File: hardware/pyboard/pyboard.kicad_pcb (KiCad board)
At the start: 2 copper layers, 65 parts, among them J1 Battery, J2 Arduino_Mega2560_Shield, J6 USB_B_Micro, J9 Micro_SD_SCHA5B0200, Q1 IRLML6402, Q2 IRLML6402, SW1 RST, SW2 USR, U1 STM32F405RGT6, U2 MCP1703A-3302_SOT89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

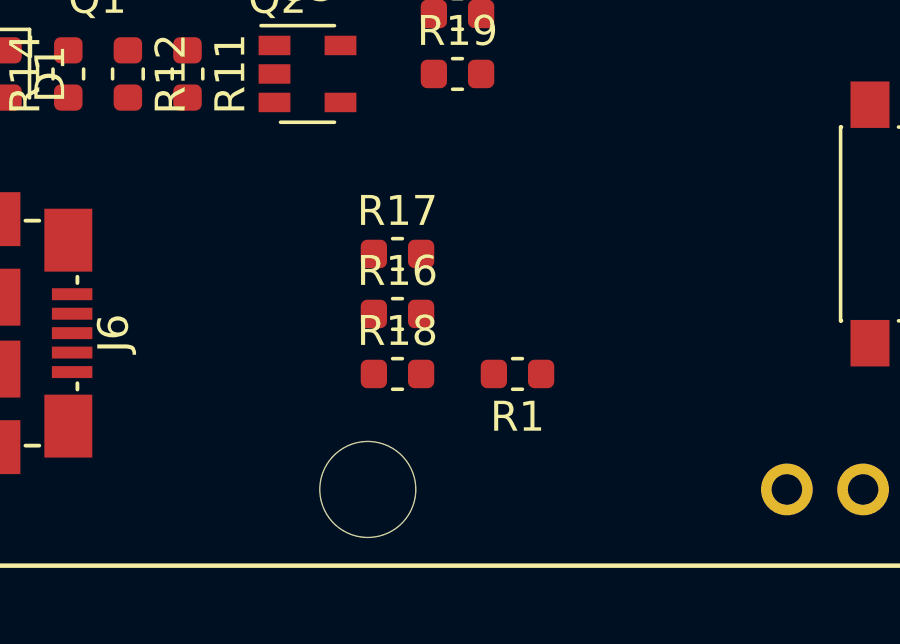
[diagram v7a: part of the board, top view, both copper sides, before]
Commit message: Configure track width
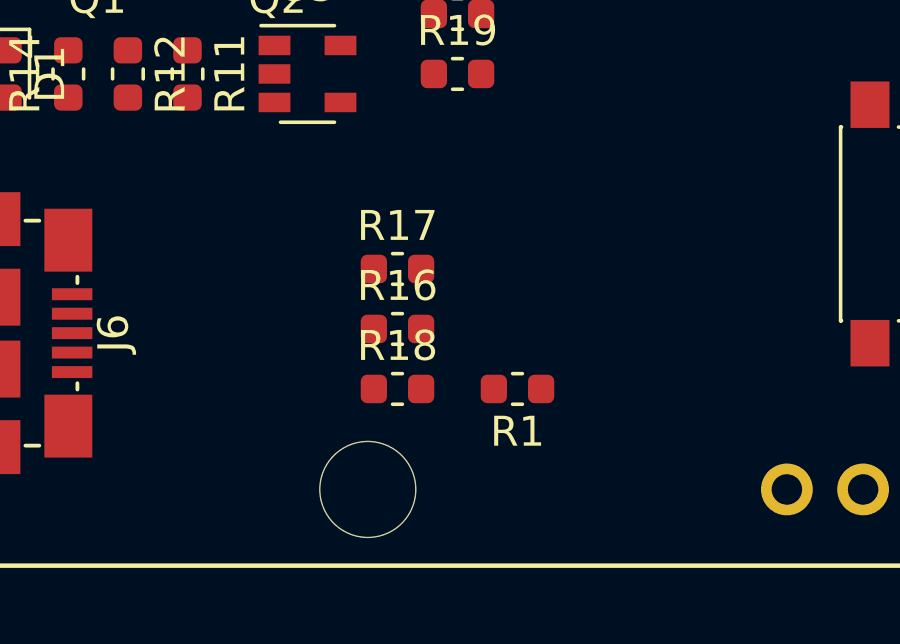
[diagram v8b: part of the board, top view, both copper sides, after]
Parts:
- moved R1 0.50 mm to (119.0, 114.1)
- moved R16 0.50 mm to (115.0, 112.1)
- moved R17 0.50 mm to (115.0, 110.1)
- moved R18 0.50 mm to (115.0, 114.1)
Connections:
- J6 pad D+: (no net) -> /DP_USB
- J6 pad D-: (no net) -> /DM_USB
- J6 pad GND: (no net) -> GND
- J6 pad ID: (no net) -> /ID_USB
- J6 pad VBUS: (no net) -> /VBUS_USB
- R16 pad 1: (no net) -> /DP_USB
- R17 pad 1: (no net) -> /DM_USB
- R18 pad 1: (no net) -> /ID_USB
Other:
- net class Default: trace_width 0.25 -> 0.3
- net class Power added: clearance 0.2, trace_width 0.8, via_dia 0.8, via_drill 0.4
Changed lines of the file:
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@@
     (zones 0)
     (modules 65)
-    (nets 73)
+    (nets 76)
   )
   (page A4)
@@
     (0 F.Cu signal)
     (31 B.Cu signal)
-    (32 B.Adhes user)
     (33 F.Adhes user)
-    (34 B.Paste user)
     (35 F.Paste user)
-    (36 B.SilkS user)
     (37 F.SilkS user)
-    (38 B.Mask user)
     (39 F.Mask user)
     (40 Dwgs.User user)
@@
     (46 B.CrtYd user)
     (47 F.CrtYd user)
-    (48 B.Fab user)
-    (49 F.Fab user hide)
+    (49 F.Fab user)
   )
   (setup
-    (last_trace_width 0.25)
+    (last_trace_width 0.3)
     (trace_clearance 0.2)
     (zone_clearance 0.508)
@@
     (mod_text_size 1 1)
     (mod_text_width 0.15)
-    (pad_size 1.89992 1.89992)
+    (pad_size 0.875 0.95)
     (pad_drill 0)
     (pad_to_mask_clearance 0.051)
     (solder_mask_min_width 0.25)
     (aux_axis_origin 0 0)
-    (grid_origin 99.96 66.61)
-    (visible_elements FFFFFF7F)
+    (visible_elements FFFDFF7F)
     (pcbplotparams
       (layerselection 0x010fc_ffffffff)
@@
   (net 71 /DM)
   (net 72 /VBUS_USB)
+  (net 73 /DP_USB)
+  (net 74 /DM_USB)
+  (net 75 /ID_USB)
   (net_class Default "This is the default net class."
     (clearance 0.2)
-    (trace_width 0.25)
+    (trace_width 0.3)
     (via_dia 0.8)
     (via_drill 0.4)
     (uvia_dia 0.3)
     (uvia_drill 0.1)
-    (add_net +3V3)
     (add_net /B)
     (add_net /BLU)
@@
     (add_net /VCAP_1)
     (add_net /VCAP_2)
-    (add_net /VRTC)
     (add_net /X1)
     (add_net /X11)
@@
     (add_net /~OC)
     (add_net /~RST)
-    (add_net GND)
     (add_net "Net-(C12-Pad2)")
     (add_net "Net-(C15-Pad2)")
@@
     (add_net "Net-(J1-Pad1)")
     (add_net "Net-(J2-Pad5V4)")
-    (add_net "Net-(J2-PadA14)")
-    (add_net "Net-(J2-PadA15)")
-    (add_net "Net-(J2-PadAREF)")
-    (add_net "Net-(J2-PadD16)")
-    (add_net "Net-(J2-PadD17)")
-    (add_net "Net-(J2-PadD18)")
-    (add_net "Net-(J2-PadD19)")
-    (add_net "Net-(J2-PadD22)")
-    (add_net "Net-(J2-PadD23)")
-    (add_net "Net-(J2-PadD24)")
-    (add_net "Net-(J2-PadD25)")
-    (add_net "Net-(J2-PadD26)")
-    (add_net "Net-(J2-PadD27)")
-    (add_net "Net-(J2-PadD28)")
-    (add_net "Net-(J2-PadD29)")
-    (add_net "Net-(J2-PadD30)")
-    (add_net "Net-(J2-PadD31)")
-    (add_net "Net-(J2-PadD32)")
-    (add_net "Net-(J2-PadD33)")
-    (add_net "Net-(J2-PadD34)")
-    (add_net "Net-(J2-PadD35)")
-    (add_net "Net-(J2-PadD36)")
-    (add_net "Net-(J2-PadD37)")
-    (add_net "Net-(J2-PadD38)")
-    (add_net "Net-(J2-PadD39)")
-    (add_net "Net-(J2-PadD40)")
-    (add_net "Net-(J2-PadD41)")
-    (add_net "Net-(J2-PadD42)")
-    (add_net "Net-(J2-PadD43)")
-    (add_net "Net-(J2-PadD44)")
-    (add_net "Net-(J2-PadD45)")
-    (add_net "Net-(J2-PadD46)")
-    (add_net "Net-(J2-PadD47)")
-    (add_net "Net-(J2-PadD48)")
-    (add_net "Net-(J2-PadD49)")
-    (add_net "Net-(J2-PadD50)")
-    (add_net "Net-(J2-PadD51)")
-    (add_net "Net-(J2-PadD52)")
-    (add_net "Net-(J2-PadD53)")
-    (add_net "Net-(J2-PadIORF)")
     (add_net "Net-(Q1-Pad1)")
     (add_net "Net-(Q1-Pad3)")
+    (add_net VDDA)
+  )
+  (net_class Power ""
+    (clearance 0.2)
+    (trace_width 0.8)
+    (via_dia 0.8)
+    (via_drill 0.4)
+    (uvia_dia 0.3)
+    (uvia_drill 0.1)
+    (add_net +3V3)
+    (add_net /VRTC)
+    (add_net GND)
     (add_net VCC)
-    (add_net VDDA)
   )
   (module components:Arduino_Mega2560_Shield locked (layer F.Cu)
@@
     )
   )
-  (module components:USB_Micro-B_10118192-0001LF locked (layer F.Cu)
+  (module components:USB_Micro-B_10118192-0001LF (layer F.Cu)
     (at 101.44 112.24984 270)
     (descr "MicroUSB type B OTG")
@@
     (pad CGND smd rect (at 3.0988 -2.54762 270) (size 2.09804 1.59766) (layers F.Cu F.Paste F.Mask))
     (pad CGND smd rect (at -3.0988 -2.54762 270) (size 2.09804 1.59766) (layers F.Cu F.Paste F.Mask))
-    (pad D+ smd rect (at 0 -2.67462 270) (size 0.39878 1.34874) (layers F.Cu F.Paste F.Mask))
-    (pad D- smd rect (at -0.6477 -2.67462 270) (size 0.39878 1.34874) (layers F.Cu F.Paste F.Mask))
-    (pad GND smd rect (at 1.29794 -2.67462 270) (size 0.39878 1.34874) (layers F.Cu F.Paste F.Mask))
-    (pad ID smd rect (at 0.6477 -2.67462 270) (size 0.39878 1.34874) (layers F.Cu F.Paste F.Mask))
-    (pad VBUS smd rect (at -1.29794 -2.67462 270) (size 0.39878 1.34874) (layers F.Cu F.Paste F.Mask))
+    (pad D+ smd rect (at 0 -2.67462 270) (size 0.39878 1.34874) (layers F.Cu F.Paste F.Mask)
+      (net 73 /DP_USB))
+    (pad D- smd rect (at -0.6477 -2.67462 270) (size 0.39878 1.34874) (layers F.Cu F.Paste F.Mask)
+      (net 74 /DM_USB))
+    (pad GND smd rect (at 1.29794 -2.67462 270) (size 0.39878 1.34874) (layers F.Cu F.Paste F.Mask)
+      (net 1 GND))
+    (pad ID smd rect (at 0.6477 -2.67462 270) (size 0.39878 1.34874) (layers F.Cu F.Paste F.Mask)
+      (net 75 /ID_USB))
+    (pad VBUS smd rect (at -1.29794 -2.67462 270) (size 0.39878 1.34874) (layers F.Cu F.Paste F.Mask)
+      (net 72 /VBUS_USB))
   )
   (module Capacitor_SMD:C_0603_1608Metric (layer F.Cu)
@@
   )
   (module Resistor_SMD:R_0603_1608Metric (layer F.Cu)
-    (at 118.96 113.61 180)
+    (at 118.96 114.11 180)
     (descr "Resistor SMD 0603 (1608 Metric), square (rectangular) end terminal, IPC_7351 nominal, (Body size source: http://www.tortai-tech.com/upload/download/2011102023233369053.pdf), generated with kicad-footprint-generator")
     (tags resistor)
@@
   )
   (module Resistor_SMD:R_0603_1608Metric (layer F.Cu)
-    (at 114.96 111.61)
+    (at 114.96 112.11)
     (descr "Resistor SMD 0603 (1608 Metric), square (rectangular) end terminal, IPC_7351 nominal, (Body size source: http://www.tortai-tech.com/upload/download/2011102023233369053.pdf), generated with kicad-footprint-generator")
     (tags resistor)
@@
     (pad 2 smd roundrect (at 0.7875 0) (size 0.875 0.95) (layers F.Cu F.Paste F.Mask) (roundrect_rratio 0.25)
       (net 70 /DP))
-    (pad 1 smd roundrect (at -0.7875 0) (size 0.875 0.95) (layers F.Cu F.Paste F.Mask) (roundrect_rratio 0.25))
+    (pad 1 smd roundrect (at -0.7875 0) (size 0.875 0.95) (layers F.Cu F.Paste F.Mask) (roundrect_rratio 0.25)
+      (net 73 /DP_USB))
     (model ${KISYS3DMOD}/Resistor_SMD.3dshapes/R_0603_1608Metric.wrl
       (at (xyz 0 0 0))
@@
   )
   (module Resistor_SMD:R_0603_1608Metric (layer F.Cu)
-    (at 114.96 109.61)
+    (at 114.96 110.11)
     (descr "Resistor SMD 0603 (1608 Metric), square (rectangular) end terminal, IPC_7351 nominal, (Body size source: http://www.tortai-tech.com/upload/download/2011102023233369053.pdf), generated with kicad-footprint-generator")
     (tags resistor)
@@
       (effects (font (size 0.4 0.4) (thickness 0.06)))
     )
-    (pad 1 smd roundrect (at -0.7875 0) (size 0.875 0.95) (layers F.Cu F.Paste F.Mask) (roundrect_rratio 0.25))
+    (pad 1 smd roundrect (at -0.7875 0) (size 0.875 0.95) (layers F.Cu F.Paste F.Mask) (roundrect_rratio 0.25)
+      (net 74 /DM_USB))
     (pad 2 smd roundrect (at 0.7875 0) (size 0.875 0.95) (layers F.Cu F.Paste F.Mask) (roundrect_rratio 0.25)
       (net 71 /DM))
@@
   )
   (module Resistor_SMD:R_0603_1608Metric (layer F.Cu)
-    (at 114.96 113.61)
+    (at 114.96 114.11)
     (descr "Resistor SMD 0603 (1608 Metric), square (rectangular) end terminal, IPC_7351 nominal, (Body size source: http://www.tortai-tech.com/upload/download/2011102023233369053.pdf), generated with kicad-footprint-generator")
     (tags resistor)
@@
     (pad 2 smd roundrect (at 0.7875 0) (size 0.875 0.95) (layers F.Cu F.Paste F.Mask) (roundrect_rratio 0.25)
       (net 65 /ID))
-    (pad 1 smd roundrect (at -0.7875 0) (size 0.875 0.95) (layers F.Cu F.Paste F.Mask) (roundrect_rratio 0.25))
+    (pad 1 smd roundrect (at -0.7875 0) (size 0.875 0.95) (layers F.Cu F.Paste F.Mask) (roundrect_rratio 0.25)
+      (net 75 /ID_USB))
     (model ${KISYS3DMOD}/Resistor_SMD.3dshapes/R_0603_1608Metric.wrl
       (at (xyz 0 0 0))
